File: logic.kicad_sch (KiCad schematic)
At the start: 79 parts, among them J10 I2C, J4 SMBUS, J5 HanRun_HR911105A, Q24 2N7002, Q25 AO3401A, SW2 SW_Push, U10 LAN8720A, U11 74HC595, U17 N066-6448TSWEG03-H28, U8 SY8120B1ABC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

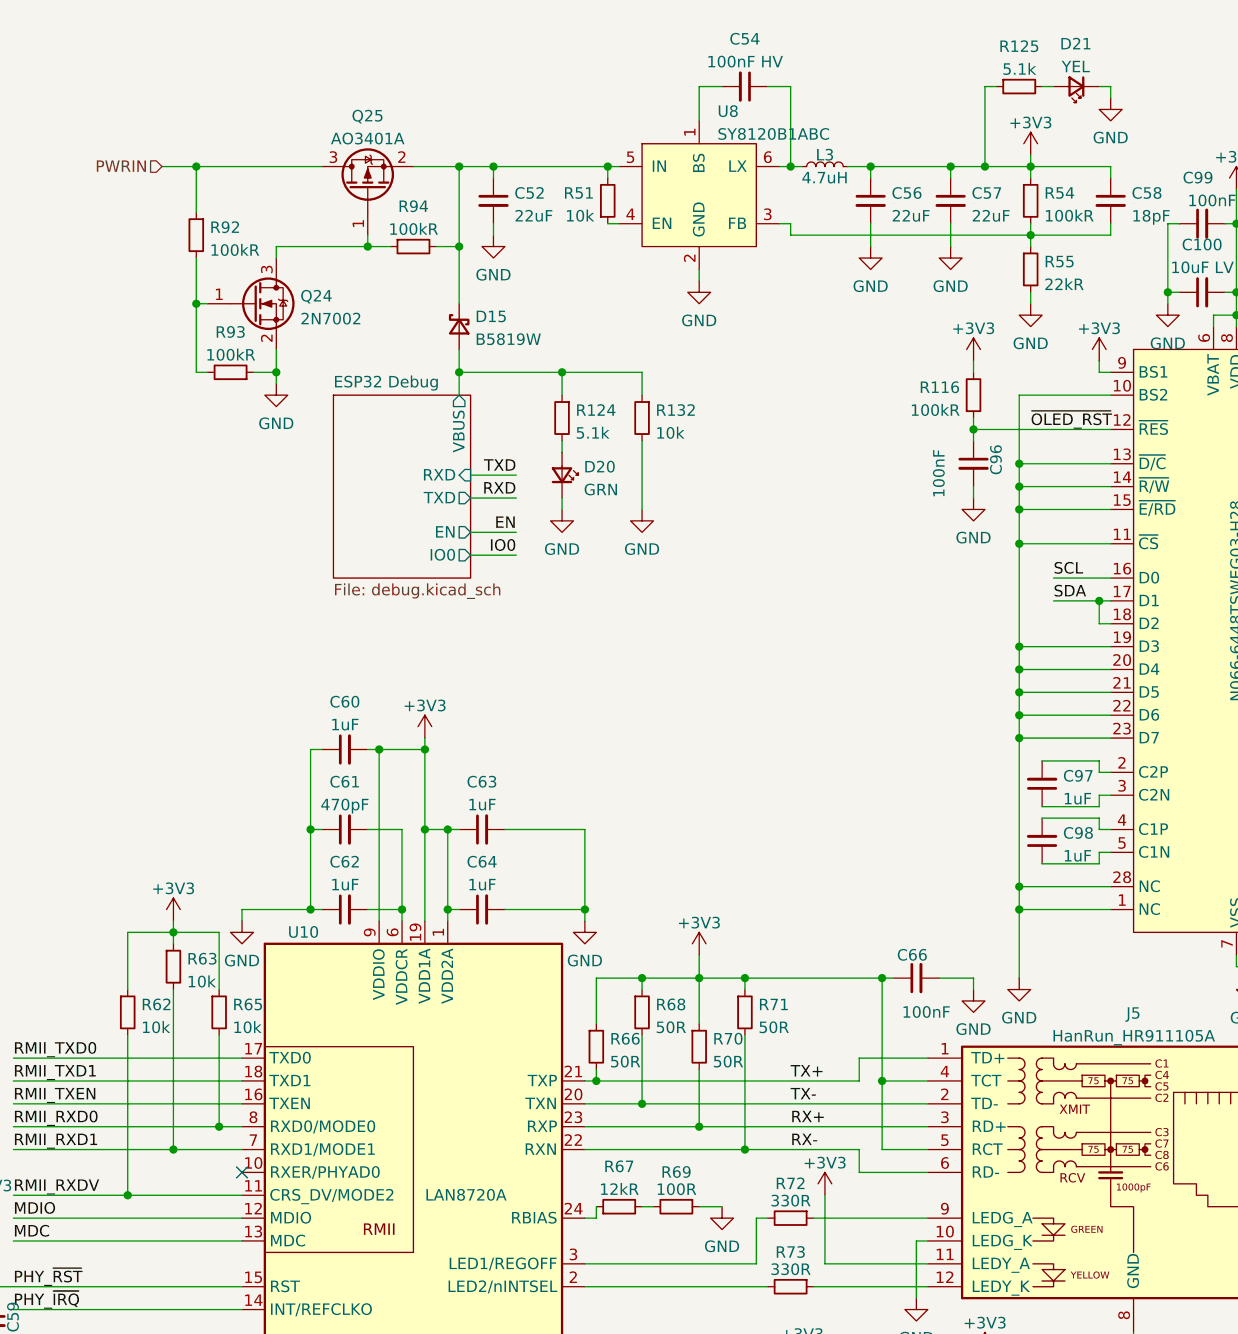
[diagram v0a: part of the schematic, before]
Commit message: Rev 1.0 bugfixes
Changes:
 - Replace DCOK-driven DC passthrough switch with ideal diode
 - Reduce INA219 series filter resistance to 1 ohm
 - Simplify debug USB power gating
 - Fix incorrect USB CC pullups
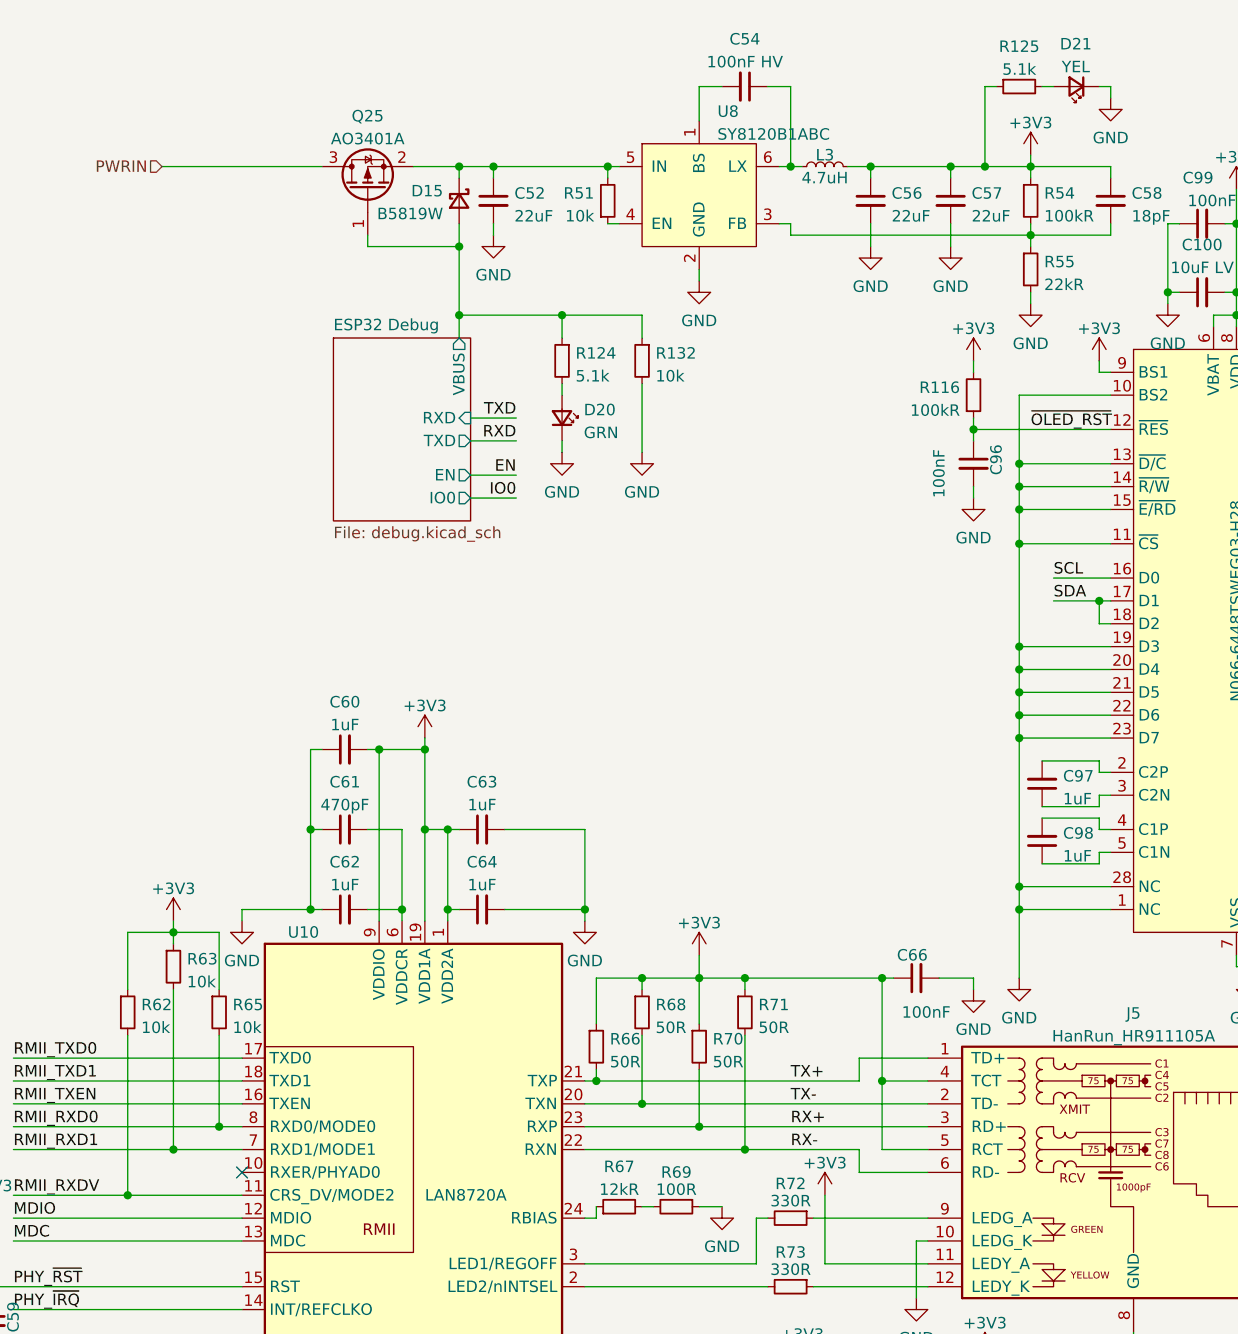
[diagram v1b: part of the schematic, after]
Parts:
- removed Q24: 2N7002, Package_TO_SOT_SMD:SOT-23, symbol Transistor_FET:2N7002
- removed R92, R93, R94: 100kR, Resistor_SMD:R_0402_1005Metric, symbol Device:R_Small
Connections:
- net ESP32 Debug/VBUS: now also Q25.1 (G)
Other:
- moved on the sheet: D15, D20, R124, R132

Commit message: Fix remaining RevB bugs
 - DNP Q13 by default to ensure uninterrupted power power delivery
 - Use lower resistance load resistors for DC step-up selftest
 - Add edge rails to support JLCPCB standard assembly

Unfortuantely JLCPCB does not seems to offer ESP32 WROOMs anymore for
economic PCBA. Thus edge-rails have been added to support standard PCBA.
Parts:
- D20: LCSC C72043 -> C2994781
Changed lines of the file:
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@@
       (effects (font (size 1.27 1.27)) hide)
     )
-    (property "LCSC" "C72043" (at 85.09 62.23 0)
+    (property "LCSC" "C2994781" (at 85.09 62.23 0)
       (effects (font (size 1.27 1.27)) hide)
     )
